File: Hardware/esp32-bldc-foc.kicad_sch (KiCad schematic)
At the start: 60 parts, among them J1 ENCODER, J2 I2C2, J3 VDRIVE, J4 MOTOR, P1 PCB_Pin_Breakout, P10 PCB_Pin_Breakout, P11 PCB_Pin_Breakout, P12 PCB_Pin_Breakout, P13 PCB_Pin_Breakout, P14 PCB_Pin_Breakout, P15 PCB_Pin_Breakout, P16 PCB_Pin_Breakout, P17 PCB_Pin_Breakout, P18 PCB_Pin_Breakout, P19 PCB_Pin_Breakout, P2 PCB_Pin_Breakout, P20 PCB_Pin_Breakout, P21 PCB_Pin_Breakout, P22 PCB_Patch, P23 PCB_Patch, P24 PCB_Patch, P25 PCB_Patch, P26 PCB_Patch, P27 PCB_Patch, P28 PCB_Patch, P29 PCB_Patch, P3 PCB_Pin_Breakout, P30 PCB_Patch, P31 PCB_Patch, P32 PCB_Patch, P33 PCB_Patch, P34 PCB_Patch, P35 PCB_Patch, P36 PCB_Patch, P37 PCB_Patch, P38 PCB_Patch, P39 PCB_Patch, P4 PCB_Pin_Breakout, P40 PCB_Patch, P5 PCB_Pin_Breakout, P6 PCB_Pin_Breakout, P7 PCB_Pin_Breakout, P8 PCB_Pin_Breakout, P9 PCB_Pin_Breakout, U1 ESP32-S3-WROOM-1, U3 SRV05-4, U6 EG2133

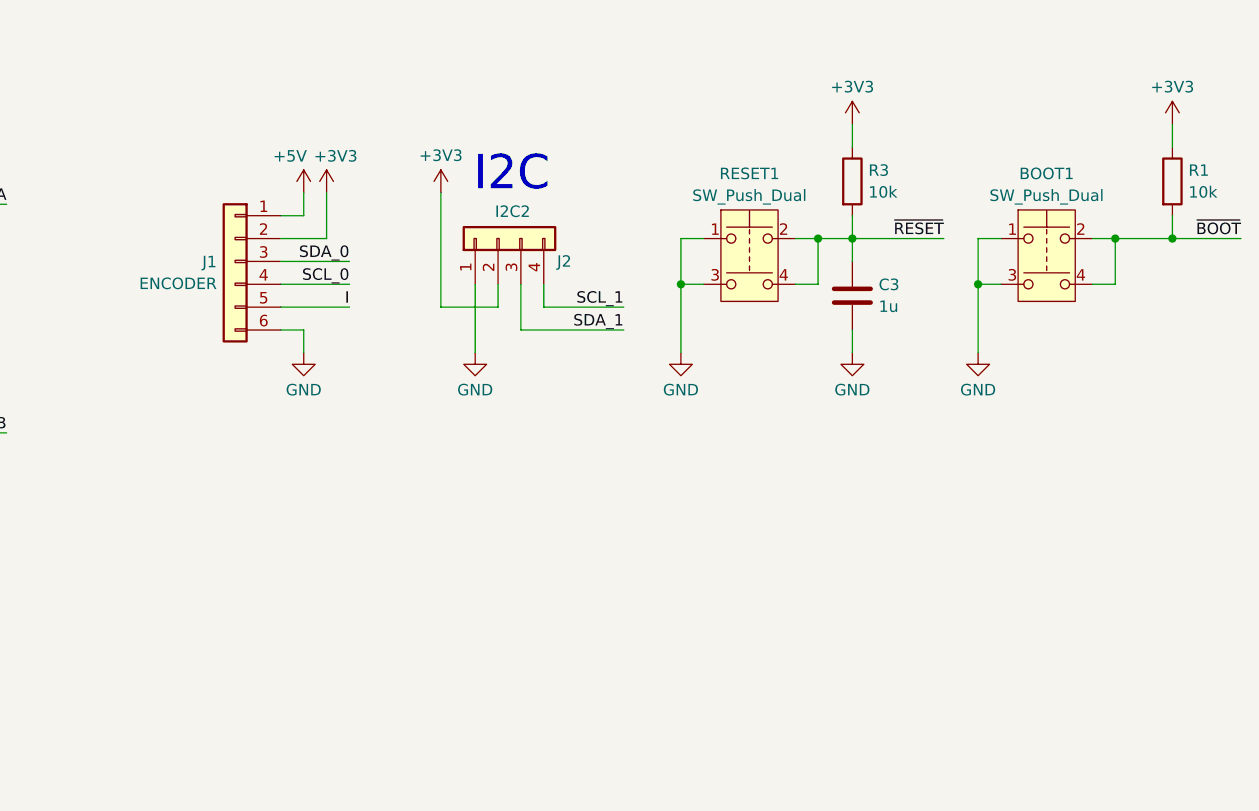
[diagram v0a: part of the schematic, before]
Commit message: Third cut of PCB.  Ready for BoM and routing
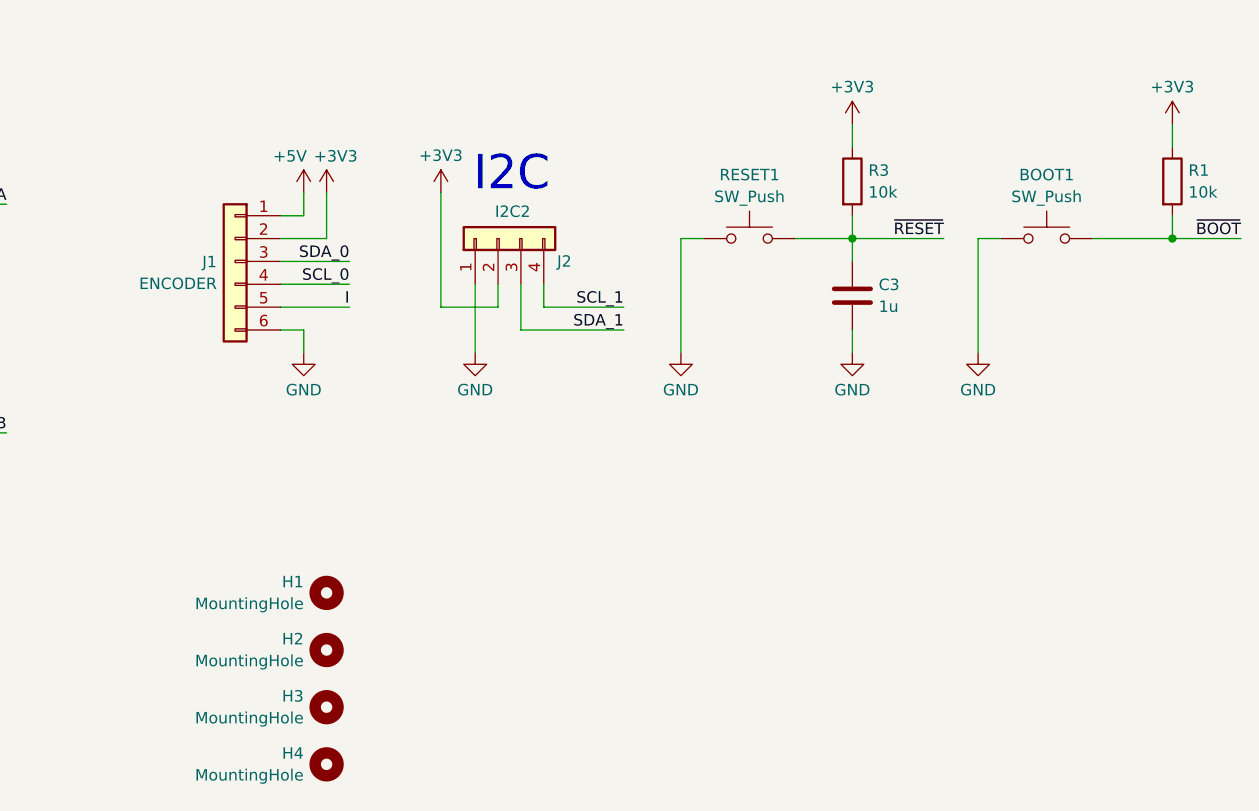
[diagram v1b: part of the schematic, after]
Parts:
- added H1, H2, H3, H4: MountingHole, MountingHole:MountingHole_3.2mm_M3_Pad, symbol afork-kicad-parts:MountingHole
- BOOT1, RESET1: value SW_Push_Dual -> SW_Push; footprint (none) -> afork-kicad-parts:SW_Push_SPST_NO_432; symbol Switch:SW_Push_Dual -> Switch:SW_Push
- C1: footprint (none) -> Capacitor_SMD:C_0603_1608Metric
- C16: footprint (none) -> Capacitor_SMD:C_1206_3216Metric
- J2: footprint Connector_JST:JST_SH_SM04B-SRSS-TB_1x04-1MP_P1.00mm_Horizontal -> afork-kicad-parts:JST_SH_SM04B-SRSS-TB_1x04-1MP_P1.00mm_Horizontal
- J3: footprint (none) -> TerminalBlock_MetzConnect:TerminalBlock_MetzConnect_Type086_RT03402HBLC_1x02_P3.81mm_Horizontal
- J4: footprint (none) -> TerminalBlock_MetzConnect:TerminalBlock_MetzConnect_Type094_RT03503HBLU_1x03_P5.00mm_Horizontal
- L1: footprint (none) -> Inductor_SMD:L_0603_1608Metric
- P1, P10, P11, P12, P13, P14, P15, P16, P17, P18, P19, P2, P20, P21, P3, P4, P5, P6, P7, P8, P9: footprint TestPoint:TestPoint_Pad_1.0x1.0mm -> afork-kicad-parts:tinySJ-Testpoint-0.7mm
- R34: footprint Resistor_SMD:R_0603_1608Metric -> Resistor_SMD:R_0805_2012Metric
- U6: footprint :TSSOP-20_L6.5-W4.4-P0.65-LS6.4-BL -> esp32-bldc-foc:TSSOP-20_L6.5-W4.4-P0.65-LS6.4-BL
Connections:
- net GND: no longer BOOT1.3, RESET1.3
- net ~{BOOT}: no longer BOOT1.4
- net ~{RESET}: no longer RESET1.4

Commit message: Remove "LCSC Part" field (I use just "LCSC")
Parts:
- U6: LCSC (none) -> C190343; LCSC Part C190343 -> (none)
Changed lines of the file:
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@@
 			)
 		)
-		(property "LCSC Part" "C190343"
-			(at 52.07 158.75 0)
+		(property "LCSC" "C190343"
+			(at 52.07 134.62 0)
 			(effects
 				(font

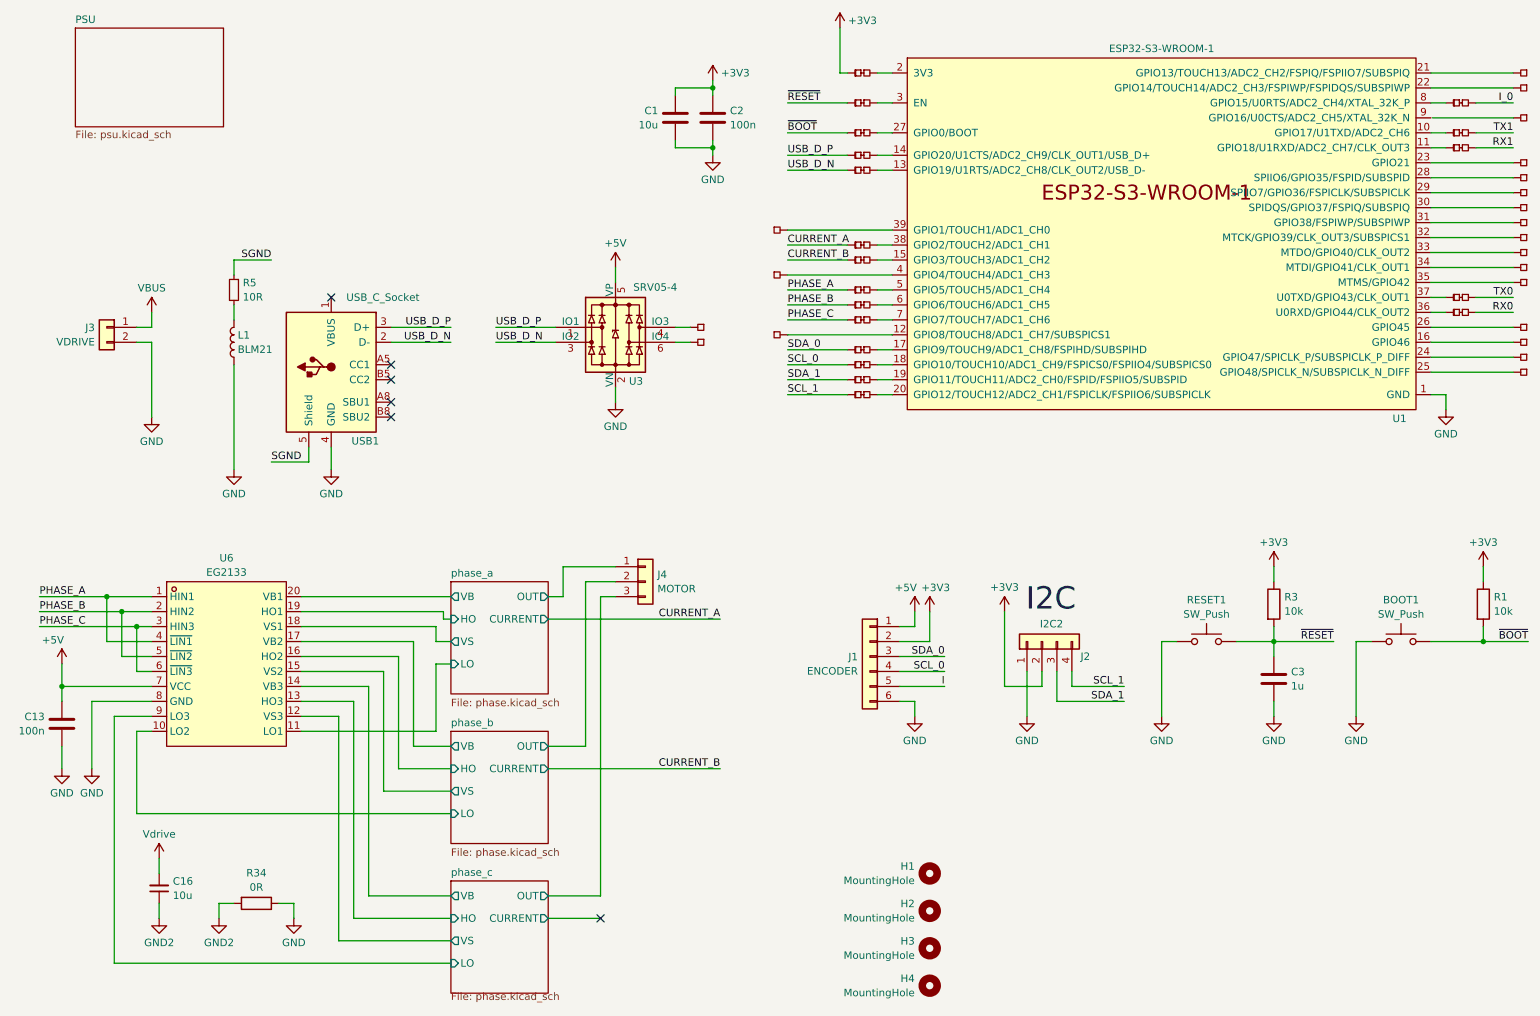
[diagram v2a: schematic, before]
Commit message: Replaced power supply with the one from OpenKayo
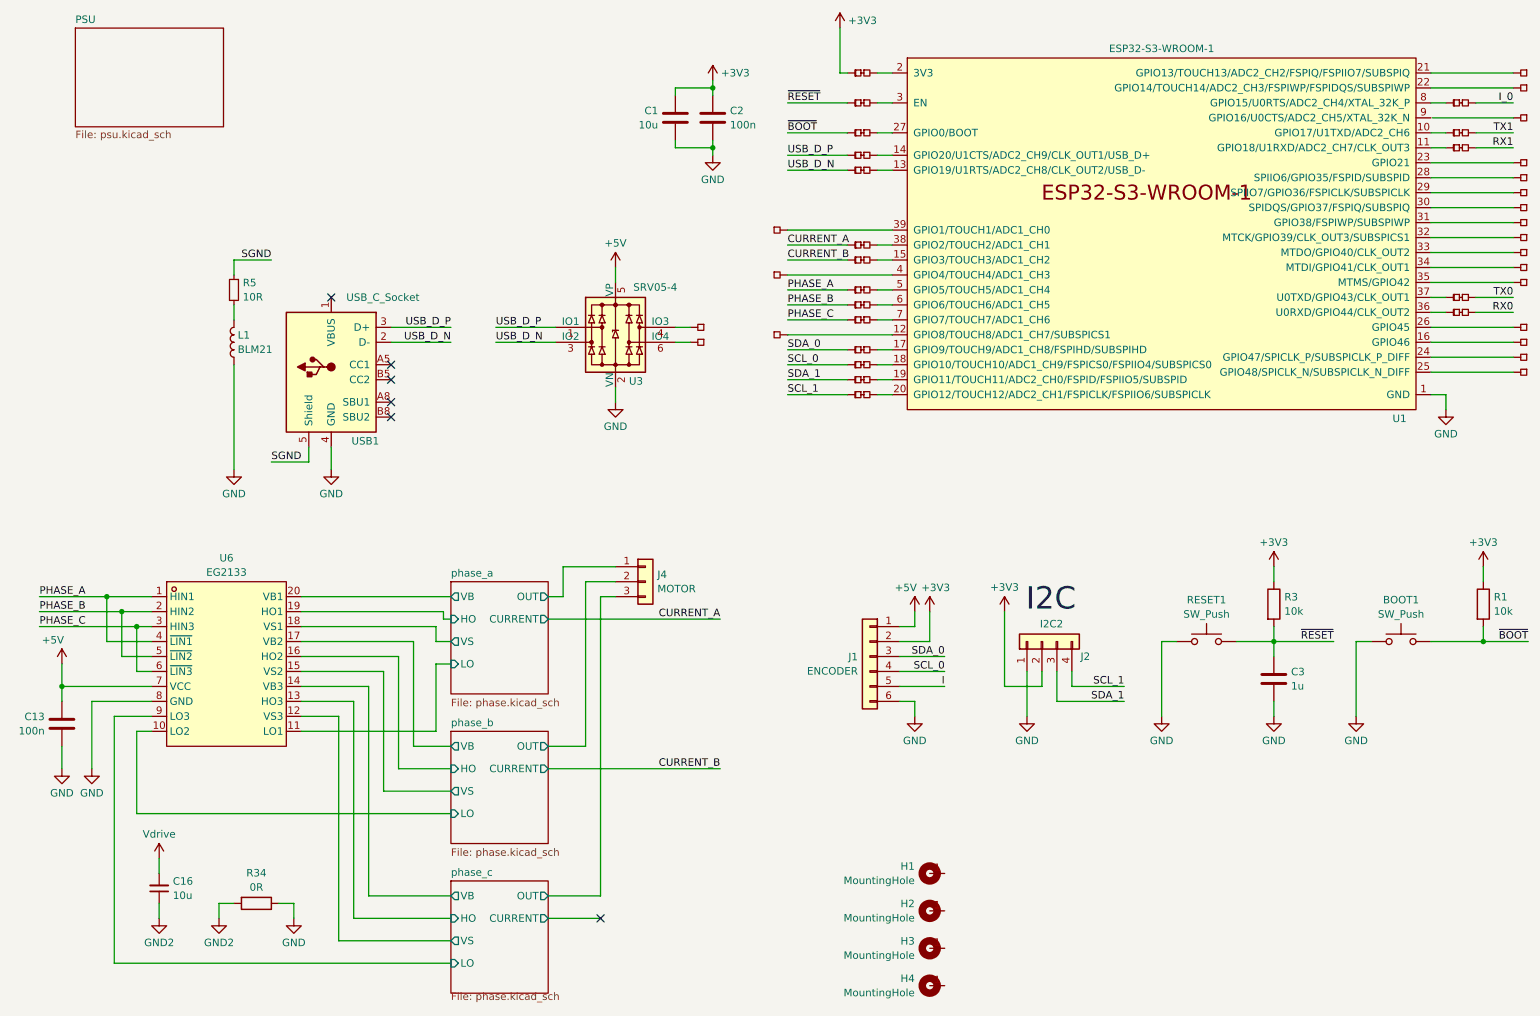
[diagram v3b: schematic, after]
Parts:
- removed J3: VDRIVE, TerminalBlock_MetzConnect:TerminalBlock_MetzConnect_Type086_RT03402HBLC_1x02_P3.81mm_Horizontal, symbol Connector_Generic:Conn_01x02
- C1: footprint Capacitor_SMD:C_0603_1608Metric -> Capacitor_SMD:C_0805_2012Metric
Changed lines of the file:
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@@
 	(wire
 		(pts
-			(xy 36.83 80.01) (xy 39.37 80.01)
-		)
-		(stroke
-			(width 0)
-			(type default)
-		)
-	)
-	(wire
-		(pts
 			(xy 256.54 36.83) (xy 270.51 36.83)
 		)
@@
 	(wire
 		(pts
-			(xy 36.83 77.47) (xy 39.37 77.47)
-		)
-		(stroke
-			(width 0)
-			(type default)
-		)
-	)
-	(wire
-		(pts
 			(xy 134.62 35.56) (xy 134.62 36.83)
 		)
@@
 	(wire
 		(pts
-			(xy 39.37 80.01) (xy 39.37 92.71)
-		)
-		(stroke
-			(width 0)
-			(type default)
-		)
-	)
-	(wire
-		(pts
 			(xy 39.37 146.05) (xy 36.83 146.05)
 		)
@@
 	(wire
 		(pts
-			(xy 39.37 77.47) (xy 39.37 74.93)
-		)
-		(stroke
-			(width 0)
-			(type default)
-		)
-	)
-	(wire
-		(pts
 			(xy 87.63 146.05) (xy 87.63 134.62)
 		)
@@
 	)
 	(symbol
-		(lib_id "power:VBUS")
-		(at 39.37 74.93 0)
-		(unit 1)
-		(exclude_from_sim no)
-		(in_bom yes)
-		(on_board yes)
-		(dnp no)
-		(fields_autoplaced yes)
-		(property "Reference" "#PWR01004"
-			(at 39.37 78.74 0)
-			(effects
-				(font
-					(size 1.27 1.27)
-				)
-				(hide yes)
-			)
-		)
-		(property "Value" "VBUS"
-			(at 39.37 70.7969 0)
-			(effects
-				(font
-					(size 1.27 1.27)
-				)
-			)
-		)
-		(property "Footprint" ""
-			(at 39.37 74.93 0)
-			(effects
-				(font
-					(size 1.27 1.27)
-				)
-				(hide yes)
-			)
-		)
-		(property "Datasheet" ""
-			(at 39.37 74.93 0)
-			(effects
-				(font
-					(size 1.27 1.27)
-				)
-				(hide yes)
-			)
-		)
-		(property "Description" "Power symbol creates a global label with name \"VBUS\""
-			(at 39.37 74.93 0)
-			(effects
-				(font
-					(size 1.27 1.27)
-				)
-				(hide yes)
-			)
-		)
-		(pin "1"
-		)
-		(instances
-			(project "esp32-bldc-foc"
-				(path "/5fd9cc58-24f5-445f-b12c-0418263ff67c"
-					(reference "#PWR01004")
-					(unit 1)
-				)
-			)
-		)
-	)
-	(symbol
 		(lib_id "afork-kicad-parts:PCB_Pin_Breakout")
 		(at 273.05 77.47 0)
@@
 	)
 	(symbol
-		(lib_id "power:GND")
-		(at 39.37 92.71 0)
-		(unit 1)
-		(exclude_from_sim no)
-		(in_bom yes)
-		(on_board yes)
-		(dnp no)
-		(fields_autoplaced yes)
-		(property "Reference" "#PWR01005"
-			(at 39.37 99.06 0)
-			(effects
-				(font
-					(size 1.27 1.27)
-				)
-				(hide yes)
-			)
-		)
-		(property "Value" "GND"
-			(at 39.37 96.8431 0)
-			(effects
-				(font
-					(size 1.27 1.27)
-				)
-			)
-		)
-		(property "Footprint" ""
-			(at 39.37 92.71 0)
-			(effects
-				(font
-					(size 1.27 1.27)
-				)
-				(hide yes)
-			)
-		)
-		(property "Datasheet" ""
-			(at 39.37 92.71 0)
-			(effects
-				(font
-					(size 1.27 1.27)
-				)
-				(hide yes)
-			)
-		)
-		(property "Description" "Power symbol creates a global label with name \"GND\" , ground"
-			(at 39.37 92.71 0)
-			(effects
-				(font
-					(size 1.27 1.27)
-				)
-				(hide yes)
-			)
-		)
-		(pin "1"
-		)
-		(instances
-			(project "esp32-bldc-foc"
-				(path "/5fd9cc58-24f5-445f-b12c-0418263ff67c"
-					(reference "#PWR01005")
-					(unit 1)
-				)
-			)
-		)
-	)
-	(symbol
 		(lib_id "Connector_Generic:Conn_01x06")
 		(at 161.29 133.35 0)
@@
 			)
 		)
-		(property "Footprint" "Capacitor_SMD:C_0603_1608Metric"
+		(property "Footprint" "Capacitor_SMD:C_0805_2012Metric"
 			(at 127.3048 45.72 0)
 			(effects
@@
 	)
 	(symbol
-		(lib_id "Connector_Generic:Conn_01x02")
-		(at 31.75 77.47 0)
-		(mirror y)
-		(unit 1)
-		(exclude_from_sim no)
-		(in_bom yes)
-		(on_board yes)
-		(dnp no)
-		(property "Reference" "J3"
-			(at 29.718 77.5278 0)
-			(effects
-				(font
-					(size 1.27 1.27)
-				)
-				(justify left)
-			)
-		)
-		(property "Value" "VDRIVE"
-			(at 29.718 79.9521 0)
-			(effects
-				(font
-					(size 1.27 1.27)
-				)
-				(justify left)
-			)
-		)
-		(property "Footprint" "TerminalBlock_MetzConnect:TerminalBlock_MetzConnect_Type086_RT03402HBLC_1x02_P3.81mm_Horizontal"
-			(at 31.75 77.47 0)
-			(effects
-				(font
-					(size 1.27 1.27)
-				)
-				(hide yes)
-			)
-		)
-		(property "Datasheet" "~"
-			(at 31.75 77.47 0)
-			(effects
-				(font
-					(size 1.27 1.27)
-				)
-				(hide yes)
-			)
-		)
-		(property "Description" "Generic connector, single row, 01x02, script generated (kicad-library-utils/schlib/autogen/connector/)"
-			(at 31.75 77.47 0)
-			(effects
-				(font
-					(size 1.27 1.27)
-				)
-				(hide yes)
-			)
-		)
-		(pin "2"
-		)
-		(pin "1"
-		)
-		(instances
-			(project "esp32-bldc-foc"
-				(path "/5fd9cc58-24f5-445f-b12c-0418263ff67c"
-					(reference "J3")
-					(unit 1)
-				)
-			)
-		)
-	)
-	(symbol
 		(lib_id "afork-kicad-parts:MountingHole")
 		(at 171.45 170.18 0)
@@
 			)
 		)
+		(pin "1"
+		)
 		(instances
 			(project "esp32-bldc-foc"
@@
 			)
 		)
+		(pin "1"
+		)
 		(instances
 			(project "esp32-bldc-foc"
@@
 			)
 		)
+		(pin "1"
+		)
 		(instances
 			(project "esp32-bldc-foc"
@@
 			)
 		)
+		(pin "1"
+		)
 		(instances
